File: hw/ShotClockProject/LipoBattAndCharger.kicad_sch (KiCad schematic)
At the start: 21 parts, among them IC1 TP4056-42-ESOP8_Rearanged, J4 Conn_01x03_Pin, J5 Conn_01x02_Pin, J6 Conn_01x03_Pin, Q1 Q_PMOS_SGD

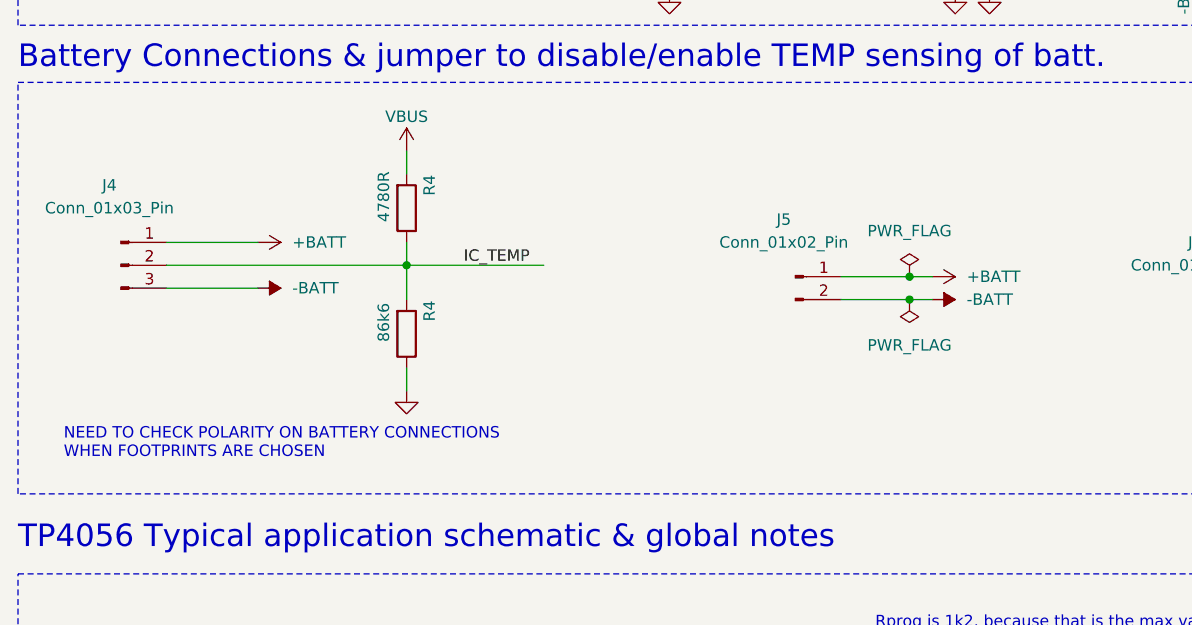
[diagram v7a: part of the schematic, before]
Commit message: Finished rough layout of PCB (ready for review)
Changed battery polarity to match the batteries I have.
Added power led to voltage regulator
Removed old comments from schematic
Gave all footprints a 3D model
Replaced batttery footprint with a SMD JST 3 pins horizontal connector
Finished rough placement of components
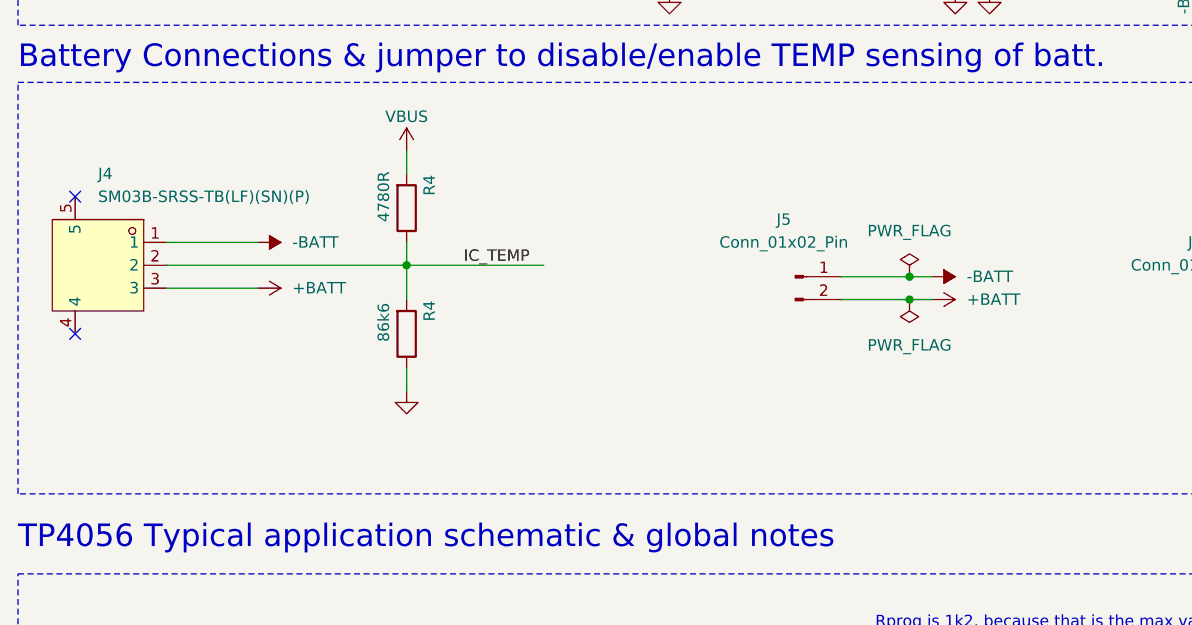
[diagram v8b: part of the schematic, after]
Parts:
- removed J4: Conn_01x03_Pin, Connector_PinHeader_1.00mm:PinHeader_1x03_P1.00mm_Horizontal, symbol Connector:Conn_01x03_Pin
- added J4: SM03B-SRSS-TB(LF)(SN)(P), SM03B-SRSS-TB:CONN-SMD_SM03B-SRSS-TB-LF-SN-P, symbol SM03B-SRSS-TB:SM03B-SRSS-TB(LF)(SN)(P)
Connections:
- net +BATT: now also J5.2 (Pin_2), J4.3; no longer J5.1 (Pin_1)
- net -BATT: now also J5.1 (Pin_1), J4.1; no longer J5.2 (Pin_2)
- net IC_TEMP: now also J4.2
- no-connect marks 1 -> 3
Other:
- note removed: "NEED TO CHECK POLARITY ON BATTERY CONNECTIONS WHEN FOOTPRINTS ARE CHOSEN"
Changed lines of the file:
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@@
   (junction (at 220.98 54.61) (diameter 0) (color 0 0 0 0)
   )
+  (no_connect (at 29.21 119.38))
+  (no_connect (at 29.21 104.14))
   (no_connect (at 160.02 115.57))
   (wire (pts (xy 66.04 109.22) (xy 66.04 111.76))
@@
     (effects (font (size 1.27 1.27)) (justify left bottom))
   )
-  (text "NEED TO CHECK POLARITY ON BATTERY CONNECTIONS \nWHEN FOOTPRINTS ARE CHOSEN"
-    (at 27.94 133.35 0)
-    (effects (font (size 1.27 1.27)) (justify left bottom))
-  )
   (text "Battery Connections & jumper to disable/enable TEMP sensing of batt."
     (at 22.86 90.17 0)
@@
     )
   )
-  (symbol (lib_id "power:+BATT") (at 49.53 109.22 270) (mirror x) (unit 1)
+  (symbol (lib_id "power:+BATT") (at 49.53 114.3 270) (mirror x) (unit 1)
     (in_bom yes) (on_board yes) (dnp no) (fields_autoplaced)
-    (property "Reference" "#PWR017" (at 45.72 109.22 0)
-      (effects (font (size 1.27 1.27)) hide)
-    )
-    (property "Value" "+BATT" (at 53.34 109.22 90)
+    (property "Reference" "#PWR017" (at 45.72 114.3 0)
+      (effects (font (size 1.27 1.27)) hide)
+    )
+    (property "Value" "+BATT" (at 53.34 114.3 90)
       (effects (font (size 1.27 1.27)) (justify left))
     )
-    (property "Footprint" "" (at 49.53 109.22 0)
-      (effects (font (size 1.27 1.27)) hide)
-    )
-    (property "Datasheet" "" (at 49.53 109.22 0)
+    (property "Footprint" "" (at 49.53 114.3 0)
+      (effects (font (size 1.27 1.27)) hide)
+    )
+    (property "Datasheet" "" (at 49.53 114.3 0)
       (effects (font (size 1.27 1.27)) hide)
     )
@@
         (path "/5fd859aa-754d-49c2-9762-3f7ebe3bb64c/d287d155-1951-4d4f-8d6c-570f03bc79f5"
           (reference "#PWR032") (unit 1)
+        )
+      )
+    )
+  )
+  (symbol (lib_id "SM03B-SRSS-TB:SM03B-SRSS-TB(LF)(SN)(P)") (at 34.29 111.76 0) (mirror y) (unit 1)
+    (in_bom yes) (on_board yes) (dnp no)
+    (property "Reference" "J4" (at 31.75 101.6 0)
+      (effects (font (size 1.27 1.27)) (justify right))
+    )
+    (property "Value" "SM03B-SRSS-TB(LF)(SN)(P)" (at 31.75 104.14 0)
+      (effects (font (size 1.27 1.27)) (justify right))
+    )
+    (property "Footprint" "SM03B-SRSS-TB:CONN-SMD_SM03B-SRSS-TB-LF-SN-P" (at 34.29 127 0)
+      (effects (font (size 1.27 1.27)) hide)
+    )
+    (property "Datasheet" "https://lcsc.com/product-detail/Others_JST-Sales-America__JST-Sales-America-SM03B-SRSS-TB-LF-SN-P_C160403.html" (at 34.29 129.54 0)
+      (effects (font (size 1.27 1.27)) hide)
+    )
+    (property "Manufacturer" "JST" (at 34.29 132.08 0)
+      (effects (font (size 1.27 1.27)) hide)
+    )
+    (property "LCSC Part" "C160403" (at 34.29 134.62 0)
+      (effects (font (size 1.27 1.27)) hide)
+    )
+    (property "JLC Part" "Extended Part" (at 34.29 137.16 0)
+      (effects (font (size 1.27 1.27)) hide)
+    )
+    (pin "1")
+    (pin "2")
+    (pin "3")
+    (pin "4")
+    (pin "5")
+    (instances
+      (project "ShotClockProject"
+        (path "/5fd859aa-754d-49c2-9762-3f7ebe3bb64c/d287d155-1951-4d4f-8d6c-570f03bc79f5"
+          (reference "J4") (unit 1)
         )
       )
@@
     )
   )
-  (symbol (lib_id "Connector:Conn_01x03_Pin") (at 34.29 111.76 0) (unit 1)
-    (in_bom yes) (on_board yes) (dnp no)
-    (property "Reference" "J4" (at 33.02 102.87 0)
-      (effects (font (size 1.27 1.27)))
-    )
-    (property "Value" "Conn_01x03_Pin" (at 33.02 105.41 0)
-      (effects (font (size 1.27 1.27)))
-    )
-    (property "Footprint" "Connector_PinHeader_1.00mm:PinHeader_1x03_P1.00mm_Horizontal" (at 34.29 111.76 0)
-      (effects (font (size 1.27 1.27)) hide)
-    )
-    (property "Datasheet" "~" (at 34.29 111.76 0)
-      (effects (font (size 1.27 1.27)) hide)
-    )
-    (pin "1")
-    (pin "2")
-    (pin "3")
-    (instances
-      (project "ShotClockProject"
-        (path "/5fd859aa-754d-49c2-9762-3f7ebe3bb64c/d287d155-1951-4d4f-8d6c-570f03bc79f5"
-          (reference "J4") (unit 1)
-        )
-      )
-    )
-  )
   (symbol (lib_id "Connector:Conn_01x02_Pin") (at 109.22 113.03 0) (unit 1)
     (in_bom yes) (on_board yes) (dnp no)
@@
     )
   )
-  (symbol (lib_id "power:+BATT") (at 124.46 113.03 270) (mirror x) (unit 1)
+  (symbol (lib_id "power:+BATT") (at 124.46 115.57 270) (mirror x) (unit 1)
     (in_bom yes) (on_board yes) (dnp no) (fields_autoplaced)
-    (property "Reference" "#PWR017" (at 120.65 113.03 0)
-      (effects (font (size 1.27 1.27)) hide)
-    )
-    (property "Value" "+BATT" (at 128.27 113.03 90)
+    (property "Reference" "#PWR017" (at 120.65 115.57 0)
+      (effects (font (size 1.27 1.27)) hide)
+    )
+    (property "Value" "+BATT" (at 128.27 115.57 90)
       (effects (font (size 1.27 1.27)) (justify left))
     )
-    (property "Footprint" "" (at 124.46 113.03 0)
-      (effects (font (size 1.27 1.27)) hide)
-    )
-    (property "Datasheet" "" (at 124.46 113.03 0)
+    (property "Footprint" "" (at 124.46 115.57 0)
+      (effects (font (size 1.27 1.27)) hide)
+    )
+    (property "Datasheet" "" (at 124.46 115.57 0)
       (effects (font (size 1.27 1.27)) hide)
     )
@@
     )
   )
-  (symbol (lib_id "power:-BATT") (at 49.53 114.3 270) (mirror x) (unit 1)
+  (symbol (lib_id "power:-BATT") (at 49.53 109.22 270) (mirror x) (unit 1)
     (in_bom yes) (on_board yes) (dnp no) (fields_autoplaced)
-    (property "Reference" "#PWR018" (at 45.72 114.3 0)
-      (effects (font (size 1.27 1.27)) hide)
-    )
-    (property "Value" "-BATT" (at 53.34 114.3 90)
+    (property "Reference" "#PWR018" (at 45.72 109.22 0)
+      (effects (font (size 1.27 1.27)) hide)
+    )
+    (property "Value" "-BATT" (at 53.34 109.22 90)
       (effects (font (size 1.27 1.27)) (justify left))
     )
-    (property "Footprint" "" (at 49.53 114.3 0)
-      (effects (font (size 1.27 1.27)) hide)
-    )
-    (property "Datasheet" "" (at 49.53 114.3 0)
+    (property "Footprint" "" (at 49.53 109.22 0)
+      (effects (font (size 1.27 1.27)) hide)
+    )
+    (property "Datasheet" "" (at 49.53 109.22 0)
       (effects (font (size 1.27 1.27)) hide)
     )
@@
     )
   )
-  (symbol (lib_id "power:-BATT") (at 124.46 115.57 270) (mirror x) (unit 1)
+  (symbol (lib_id "power:-BATT") (at 124.46 113.03 270) (mirror x) (unit 1)
     (in_bom yes) (on_board yes) (dnp no) (fields_autoplaced)
-    (property "Reference" "#PWR018" (at 120.65 115.57 0)
-      (effects (font (size 1.27 1.27)) hide)
-    )
-    (property "Value" "-BATT" (at 128.27 115.57 90)
+    (property "Reference" "#PWR018" (at 120.65 113.03 0)
+      (effects (font (size 1.27 1.27)) hide)
+    )
+    (property "Value" "-BATT" (at 128.27 113.03 90)
       (effects (font (size 1.27 1.27)) (justify left))
     )
-    (property "Footprint" "" (at 124.46 115.57 0)
-      (effects (font (size 1.27 1.27)) hide)
-    )
-    (property "Datasheet" "" (at 124.46 115.57 0)
-      (effects (font (size 1.27 1.27)) hide)
-    )
+    (property "Footprint" "" (at 124.46 113.03 0)
+      (effects (font (size 1.27 1.27)) hide)
+    )
+    (property "Datasheet" "" (at 124.46 113.03 0)
+      (effects (font (size 1.27 1.27)) hide)
+    )
